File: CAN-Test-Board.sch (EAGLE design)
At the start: 54 parts, among them Y1 ECS-80-S-4X, Y2 ECS-80-S-4X

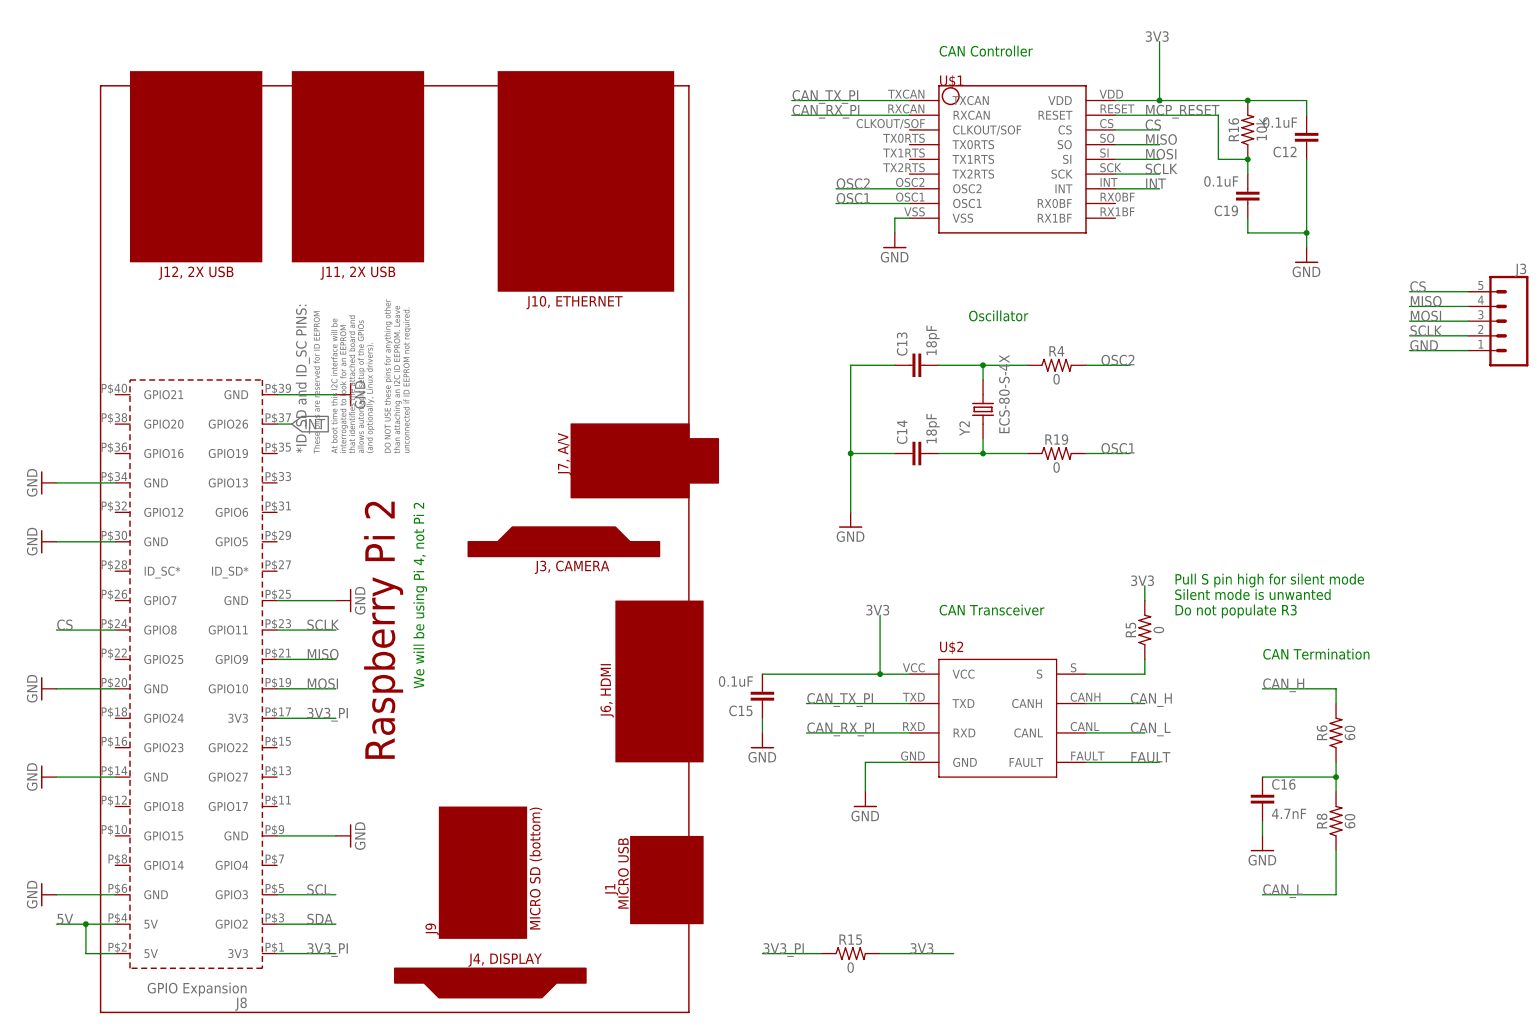
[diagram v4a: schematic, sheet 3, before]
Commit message: Update parts and values. Fix missing connection?
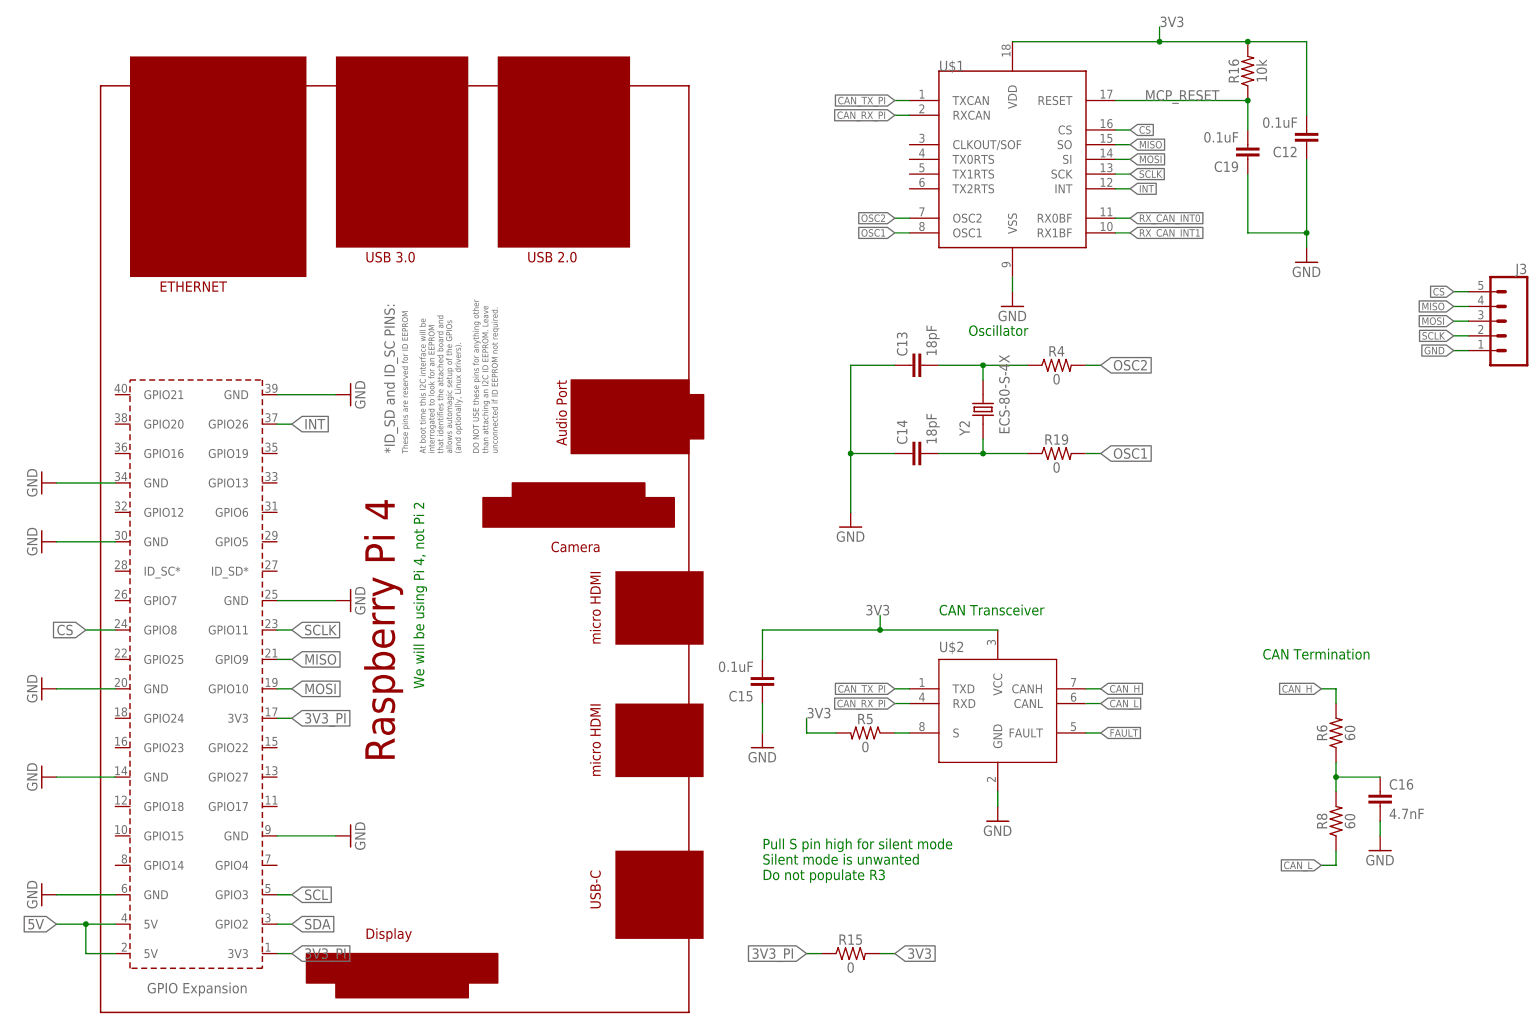
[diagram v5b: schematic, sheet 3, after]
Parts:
- removed C4, C6: 4.7uF, SparkFun-Capacitors:4.7UF0603
- C10, C2, C3, C5: value 4.7uF -> 0.1uF
- C8, C9: value 4.7uF -> 18pF
- PCB1: value RPI2 -> RPI4; device MicrocontrollerComponents:RPI2 -> AUX, RaspberryPi:RPI4
- R1, R3: value 1k -> 0
- U$1: device PI_Shield_Library:MCP2515 -> IC, STM and CAN parts:MCP2515
- U$2, U$8: device PI_Shield_Library:TCAN337D -> IC, STM and CAN parts:TCAN337D
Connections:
- net N$3 renamed OSC_2_MID
- net N$4 renamed OSC_1_MID
- net N$6 renamed SILENT_PI
- new net RX_CAN_INT0: U$1.RX0BF
- new net RX_CAN_INT1: U$1.RX1BF
- net 3V3: no longer C4.1, C6.1
- net GND: no longer C4.2, C6.2
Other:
- note removed: "CAN Controller"
- moved on the sheet: C10, C15, C16, C19, C8, C9, R1, R16, R3, R5, U$2, U$8
